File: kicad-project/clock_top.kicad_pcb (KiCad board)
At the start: 2 copper layers, 147.5 x 53.8 mm, 61 parts, among them SW1 PEC16, U1 ZS-042, U2 ZS-040, U3 KPC452, U4 KPC452, U5 KPC452, U6 KPC452

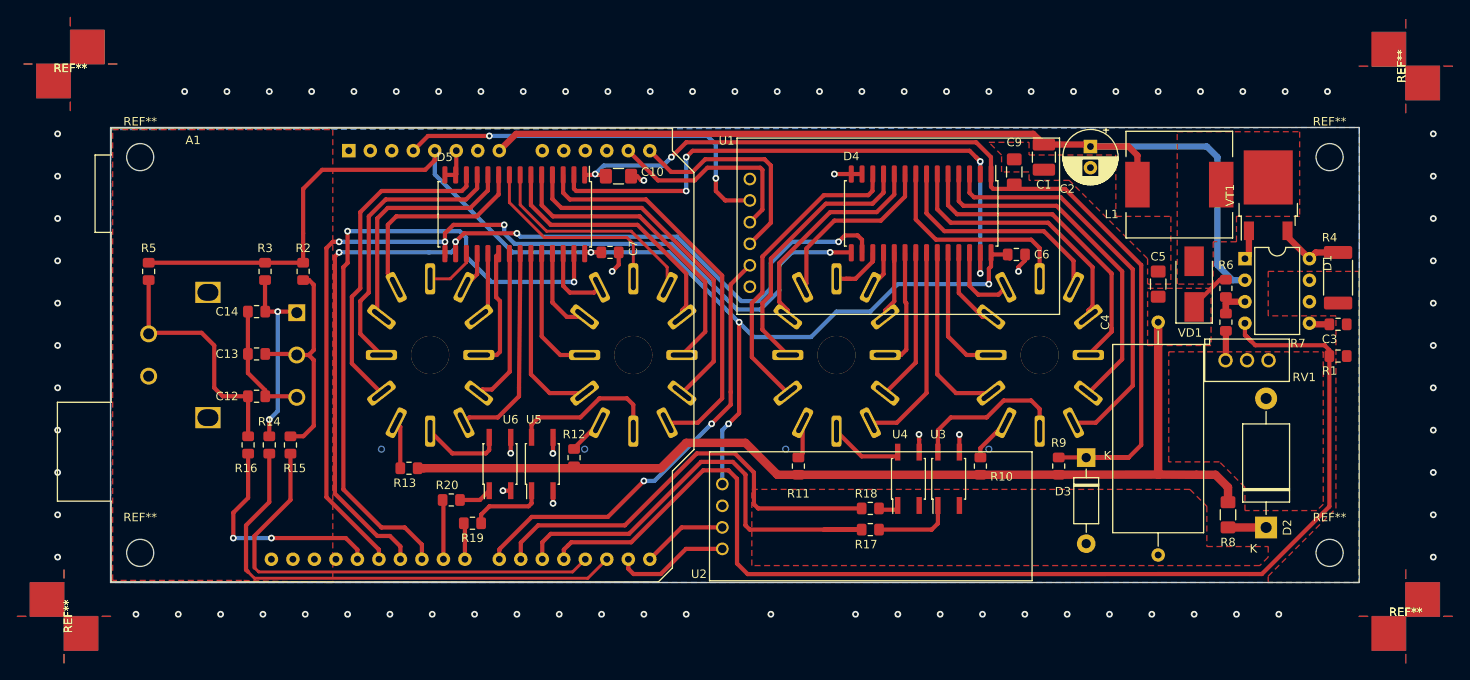
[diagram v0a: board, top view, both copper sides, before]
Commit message: git repo refactor: v2 in12, 6 tubes, arduino
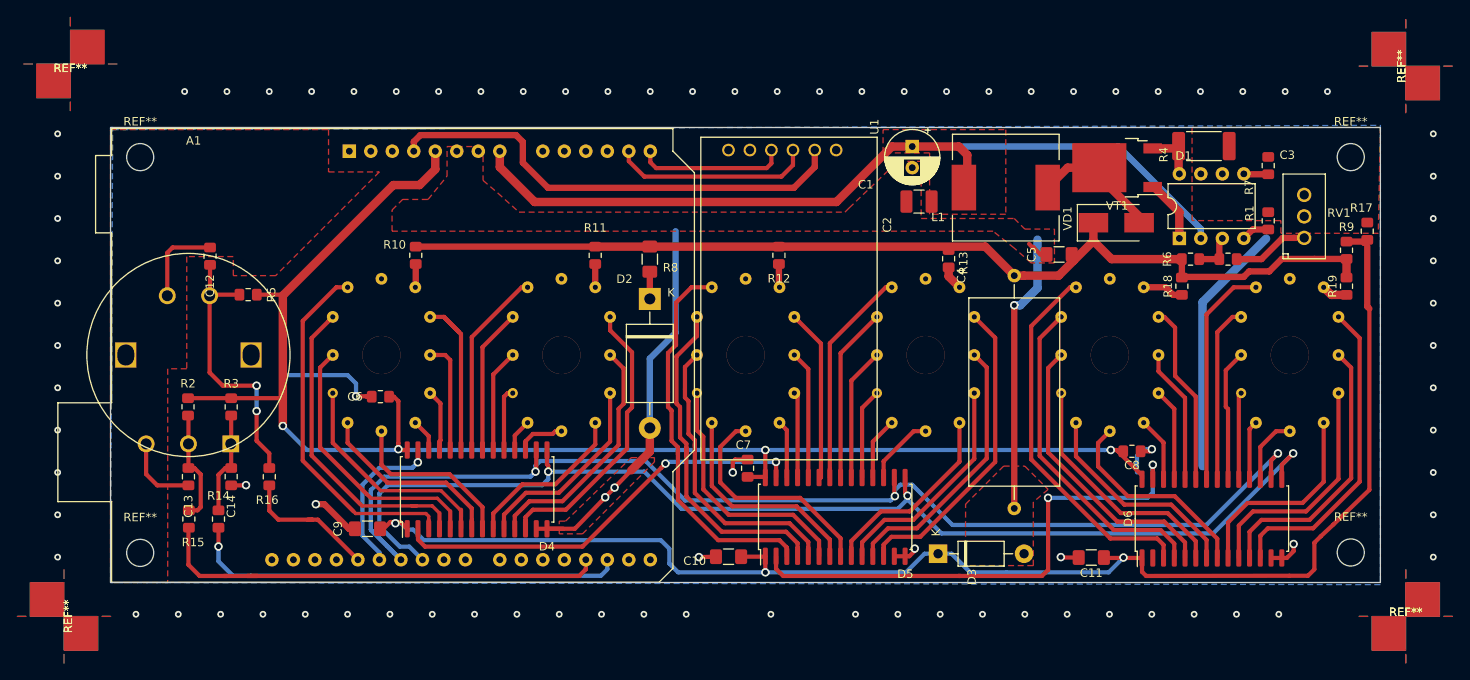
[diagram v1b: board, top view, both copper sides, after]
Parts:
- removed R20: 2.2K, Resistor_SMD:R_0805_2012Metric_Pad1.15x1.40mm_HandSolder
- removed the REF** at (240.2, 119.5)
- removed the REF** at (240.2, 72.8)
- removed U2: ZS-040, clock:zs-040
- removed U3, U4, U5, U6: KPC452, Package_SO:SO-4_4.4x3.6mm_P2.54mm
- added C11: 100nF, 250V, Capacitor_SMD:C_1206_3216Metric_Pad1.42x1.75mm_HandSolder, F.Cu at (212.1, 120.0)
- added C8: 100nF, 50V, Capacitor_SMD:C_0805_2012Metric_Pad1.15x1.40mm_HandSolder, F.Cu at (216.9, 107.5)
- added D6: HV5812, Package_SO:SOIC-28W_7.5x17.9mm_P1.27mm, F.Cu at (226.3, 115.5)
- added LL5: IN-12B, v2:IN12-HI_IE, B.Cu at (214.3, 96.1)
- added LL6: IN-12B, v2:IN12-HI_IE, B.Cu at (235.6, 96.1)
- added REF**: MountingHole_3.2mm_M3, MountingHole:MountingHole_3.2mm_M3, F.Cu at (242.8, 119.5)
- added REF**: MountingHole_3.2mm_M3, MountingHole:MountingHole_3.2mm_M3, F.Cu at (242.8, 72.8)
- LL1, LL2, LL3, LL4: footprint clock:PL31 -> v2:IN12-HI_IE
- R17: value 2.2K -> 150K
- R18, R19: value 2.2K -> 22K
- moved R19 107.0 mm to (242.2, 88.0), turned to 90 degrees
- moved C9 87.3 mm to (126.6, 116.7), turned to 180 degrees
- moved LL1 77.8 mm to (128.2, 96.1), turned to 0 degrees
- moved D2 77.6 mm to (159.9, 89.5), turned to 270 degrees
- moved C6 77.0 mm to (128.1, 101.0), turned to 0 degrees
- moved R8 74.7 mm to (159.9, 84.8)
- moved R10 71.2 mm to (132.3, 84.3), turned to 90 degrees
- moved R17 68.5 mm to (244.7, 81.5), turned to 270 degrees
- moved R13 68.4 mm to (195.2, 84.8), turned to 90 degrees
- moved D4 61.8 mm to (139.6, 112.0), turned to 90 degrees
- moved LL4 58.5 mm to (192.5, 96.1), turned to 0 degrees
- moved D5 52.1 mm to (181.8, 115.2), turned to 90 degrees
- moved C10 46.8 mm to (169.2, 120.0), turned to 180 degrees
- moved R18 45.2 mm to (222.8, 88.0), turned to 90 degrees
- moved R9 42.5 mm to (242.2, 83.8)
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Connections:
- A1 pad 15: /RxD -> Net-(A1-Pad15)
- A1 pad 16: /TxD -> Net-(A1-Pad16)
- A1 pad 19: /SHUT -> Net-(A1-Pad19)
- A1 pad 20: /_1-. -> Net-(A1-Pad20)
- A1 pad 21: /_2-. -> Net-(A1-Pad21)
- A1 pad 22: /RT_INT -> Net-(A1-Pad22)
- A1 pad 23: /_3-. -> Net-(A1-Pad23)
- A1 pad 24: /_4-. -> Net-(A1-Pad24)
- A1 pad 25: /DATA -> /CLOCK
- A1 pad 27: /CLOCK -> /DATA
- D4 pad 27: Net-(D4-Pad27) -> /DATA
- D5 pad 2: Net-(D4-Pad27) -> Net-(D5-Pad2)
- D5 pad 27: /DATA -> Net-(D4-Pad2)
- R17 pad 1: Net-(R17-Pad1) -> GND
- R17 pad 2: /_1-. -> HV_C
- R18 pad 2: /_2-. -> HV
- R19 pad 2: /_3-. -> HV
- U1 pad 2: /RT_INT -> Net-(U1-Pad2)
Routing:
- net /SHUT: track 141.3 -> 3.31 mm
- net GND: track 39.0 -> 171.6 mm, vias 10 -> 12
- net Net-(D4-Pad27): track 70.3 -> 0.00 mm, vias 4 -> 0
- net Net-(D5-Pad2): track 0.00 -> 61.4 mm, vias 0 -> 2
- net /DATA: track 78.3 -> 18.8 mm, vias 2 -> 1
- net HV_C: track 114.1 -> 172.1 mm, vias 2 -> 3
- net /_1-.: track 55.0 -> 0.00 mm
- net /RT_INT: track 53.0 -> 0.00 mm, vias 2 -> 0
- net /_2-.: track 51.5 -> 0.00 mm
- net Net-(D4-Pad2): track 0.00 -> 49.9 mm, vias 0 -> 2
- net /5-1: track 0.00 -> 44.3 mm
- net /5-2: track 0.00 -> 39.4 mm
- net /6-0: track 0.00 -> 37.5 mm
- net /5-3: track 0.00 -> 34.6 mm
- net /6-9: track 0.00 -> 32.9 mm
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- added copper zone on F.Cu, net +VDC
- removed copper zone on F.Cu, net HV
- removed copper zone on F.Cu, net Net-(L1-Pad2)
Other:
- board size 147.5 x 53.8 mm -> 150 x 53.8 mm
- net class 1: clearance 0.25 -> 0.5; via_dia 0.8 -> 1; via_drill 0.4 -> 0.6
- net class Default: clearance 0.25 -> 0.5; via_dia 0.8 -> 1; via_drill 0.4 -> 0.6
- net class sec: clearance 0.25 -> 0.5; via_dia 0.8 -> 1; via_drill 0.4 -> 0.6
- rule trace_clearance: 0.25 -> 0.5
